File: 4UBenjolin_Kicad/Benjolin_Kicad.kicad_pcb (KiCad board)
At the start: 2 copper layers, 177.8 x 59.9 mm, 106 parts, among them J1 Conn_01x03_Female, J10 MAINOUT, J11 PWM, J12 RUN, J13 XOR, J14 CV_1, J15 CV_2, J4 EXT.INPUT, J5 CV_F, J6 PUL2, J7 TRI1, J8 TRI2, J9 PUL1, P10R1 10k, P11R1 10k, P1R1 10k, P2R1 10k, P3R1 10k, P4R1 10k, P5R1 10k, P6R1 10k, P8R1 10k, P9R1 10k, Q1 BC547, SW1 SW_SPDT, U1 TL074, U2 TL072, U3 TL074, U4 TL074, U5 SSI2164, U6 4021, U7 L78L09_SOT89

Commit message: Added footprint for Banana Panel Cutout and built up a generic 4u Front Panel
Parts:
- removed C1, C11, C14, C16, C17: 100n, Capacitor_SMD:C_1206_3216Metric_Pad1.42x1.75mm_HandSolder
- removed C10, C5, C8: 220p, Capacitor_SMD:C_1206_3216Metric_Pad1.42x1.75mm_HandSolder
- removed C12, C13, C15, C18: 10uf, Capacitor_THT:CP_Radial_D5.0mm_P2.50mm
- removed C2, C3, C4, C9: 560p, Capacitor_SMD:C_1206_3216Metric_Pad1.42x1.75mm_HandSolder
- removed C6, C7: 1n, Capacitor_SMD:C_1206_3216Metric_Pad1.42x1.75mm_HandSolder
- removed D1, D2, D3, D4, D5, D6: 1N914, Diode_THT:D_DO-35_SOD27_P2.54mm_Vertical_AnodeUp
- removed J1: Conn_01x03_Female, Connector_PinSocket_2.54mm:PinSocket_1x03_P2.54mm_Vertical
- removed J10: MAINOUT, Connector_Audio:Jack_3.5mm_QingPu_WQP-PJ398SM_Vertical_CircularHoles
- removed J11: PWM, Connector_Audio:Jack_3.5mm_QingPu_WQP-PJ398SM_Vertical_CircularHoles
- removed J12: RUN, Connector_Audio:Jack_3.5mm_QingPu_WQP-PJ398SM_Vertical_CircularHoles
- removed J13: XOR, Connector_Audio:Jack_3.5mm_QingPu_WQP-PJ398SM_Vertical_CircularHoles
- removed J14: CV_1, Connector_Audio:Jack_3.5mm_QingPu_WQP-PJ398SM_Vertical_CircularHoles
- removed J15: CV_2, Connector_Audio:Jack_3.5mm_QingPu_WQP-PJ398SM_Vertical_CircularHoles
- removed J4: EXT.INPUT, Connector_Audio:Jack_3.5mm_QingPu_WQP-PJ398SM_Vertical_CircularHoles
- removed J5: CV_F, Connector_Audio:Jack_3.5mm_QingPu_WQP-PJ398SM_Vertical_CircularHoles
- removed J6: PUL2, Connector_Audio:Jack_3.5mm_QingPu_WQP-PJ398SM_Vertical_CircularHoles
- removed J7: TRI1, Connector_Audio:Jack_3.5mm_QingPu_WQP-PJ398SM_Vertical_CircularHoles
- removed J8: TRI2, Connector_Audio:Jack_3.5mm_QingPu_WQP-PJ398SM_Vertical_CircularHoles
- removed J9: PUL1, Connector_Audio:Jack_3.5mm_QingPu_WQP-PJ398SM_Vertical_CircularHoles
- removed P10R1, P11R1, P1R1, P2R1, P3R1, P4R1, P5R1, P6R1, P8R1, P9R1: 10k, Potentiometer_THT:Potentiometer_Alps_RK09K_Single_Vertical
- removed Q1: BC547, Package_TO_SOT_THT:TO-92_Inline
- removed R1, R16: 62k, Resistor_SMD:R_0603_1608Metric_Pad1.05x0.95mm_HandSolder
- removed R10, R17, R28, R29, R3, R30, R4, R6, R7: 51k, Resistor_SMD:R_0603_1608Metric_Pad1.05x0.95mm_HandSolder
- removed R11: 150k, Resistor_SMD:R_0603_1608Metric_Pad1.05x0.95mm_HandSolder
- removed R12, R13, R14, R33, R49: 10k, Resistor_SMD:R_0603_1608Metric_Pad1.05x0.95mm_HandSolder
- removed R15, R2, R20, R21, R22, R34, R37, R38, R39, R42, R45, R47, R48, R5, R8: 30k, Resistor_SMD:R_0603_1608Metric_Pad1.05x0.95mm_HandSolder
- removed R18, R31, R32, R35, R36, R9: 100k, Resistor_SMD:R_0603_1608Metric_Pad1.05x0.95mm_HandSolder
- removed R19, R26, R40, R41, R43, R44: 15k, Resistor_SMD:R_0603_1608Metric_Pad1.05x0.95mm_HandSolder
- removed R23, R24, R25, R46: 510r, Resistor_SMD:R_0603_1608Metric_Pad1.05x0.95mm_HandSolder
- removed R27: 1.5k, Resistor_SMD:R_0603_1608Metric_Pad1.05x0.95mm_HandSolder
- removed R50: 470k, Resistor_SMD:R_0603_1608Metric_Pad1.05x0.95mm_HandSolder
- removed SW1: SW_SPDT, Connector_PinSocket_2.54mm:PinSocket_1x03_P2.54mm_Vertical
- removed U1, U3, U4: TL074, Package_SO:SOIC-14_3.9x8.7mm_P1.27mm
- removed U2: TL072, Package_SO:SOIC-8_3.9x4.9mm_P1.27mm
- removed U5: SSI2164, Package_SO:SOIC-16_3.9x9.9mm_P1.27mm
- removed U6: 4021, Package_SO:SOIC-16_3.9x9.9mm_P1.27mm
- removed U7: L78L09_SOT89, Package_TO_SOT_THT:TO-92L_Inline
- added REF**: Banana Jack, SynthComponents:Cinch Banana Jack (Panel), F.Cu at (92.1, 128.6)
- added REF**: Banana Jack, SynthComponents:Cinch Banana Jack (Panel), F.Cu at (117.5, 109.5)
- added REF**: Banana Jack, SynthComponents:Cinch Banana Jack (Panel), F.Cu at (92.1, 109.5)
- added REF**: Banana Jack, SynthComponents:Cinch Banana Jack (Panel), F.Cu at (41.3, 128.6)
- added REF**: Banana Jack, SynthComponents:Cinch Banana Jack (Panel), F.Cu at (117.5, 147.6)
- added REF**: Banana Jack, SynthComponents:Cinch Banana Jack (Panel), F.Cu at (66.7, 128.6)
- added REF**: Banana Jack, SynthComponents:Cinch Banana Jack (Panel), F.Cu at (92.1, 166.7)
- added REF**: Banana Jack, SynthComponents:Cinch Banana Jack (Panel), F.Cu at (117.5, 128.6)
- added REF**: Banana Jack, SynthComponents:Cinch Banana Jack (Panel), F.Cu at (41.3, 52.4)
- added REF**: Banana Jack, SynthComponents:Cinch Banana Jack (Panel), F.Cu at (66.7, 52.4)
- added REF**: Banana Jack, SynthComponents:Cinch Banana Jack (Panel), F.Cu at (92.1, 52.4)
- added REF**: Banana Jack, SynthComponents:Cinch Banana Jack (Panel), F.Cu at (66.7, 166.7)
- added REF**: Banana Jack, SynthComponents:Cinch Banana Jack (Panel), F.Cu at (117.5, 71.4)
- added REF**: Banana Jack, SynthComponents:Cinch Banana Jack (Panel), F.Cu at (117.5, 90.5)
- added REF**: Banana Jack, SynthComponents:Cinch Banana Jack (Panel), F.Cu at (92.1, 90.5)
- added REF**: Banana Jack, SynthComponents:Cinch Banana Jack (Panel), F.Cu at (66.7, 90.5)
- added REF**: Banana Jack, SynthComponents:Cinch Banana Jack (Panel), F.Cu at (41.3, 90.5)
- added REF**: Banana Jack, SynthComponents:Cinch Banana Jack (Panel), F.Cu at (41.3, 71.4)
- added REF**: Banana Jack, SynthComponents:Cinch Banana Jack (Panel), F.Cu at (66.7, 71.4)
- added REF**: Banana Jack, SynthComponents:Cinch Banana Jack (Panel), F.Cu at (92.1, 71.4)
- added REF**: Banana Jack, SynthComponents:Cinch Banana Jack (Panel), F.Cu at (117.5, 52.4)
- added REF**: Banana Jack, SynthComponents:Cinch Banana Jack (Panel), F.Cu at (117.5, 33.3)
- added REF**: Banana Jack, SynthComponents:Cinch Banana Jack (Panel), F.Cu at (41.3, 166.7)
- added REF**: Banana Jack, SynthComponents:Cinch Banana Jack (Panel), F.Cu at (41.3, 33.3)
- added REF**: Banana Jack, SynthComponents:Cinch Banana Jack (Panel), F.Cu at (66.7, 33.3)
- added REF**: Banana Jack, SynthComponents:Cinch Banana Jack (Panel), F.Cu at (92.1, 33.3)
- added REF**: Banana Jack, SynthComponents:Cinch Banana Jack (Panel), F.Cu at (41.3, 147.6)
- added REF**: Banana Jack, SynthComponents:Cinch Banana Jack (Panel), F.Cu at (66.7, 147.6)
- added REF**: Banana Jack, SynthComponents:Cinch Banana Jack (Panel), F.Cu at (92.1, 147.6)
- added REF**: Banana Jack, SynthComponents:Cinch Banana Jack (Panel), F.Cu at (66.7, 109.5)
- added REF**: Banana Jack, SynthComponents:Cinch Banana Jack (Panel), F.Cu at (41.3, 109.5)
- added REF**: Banana Jack, SynthComponents:Cinch Banana Jack (Panel), F.Cu at (117.5, 166.7)
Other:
- board size 177.8 x 59.9 mm -> 107.9 x 177.5 mm
- board text added: "4mm hole"

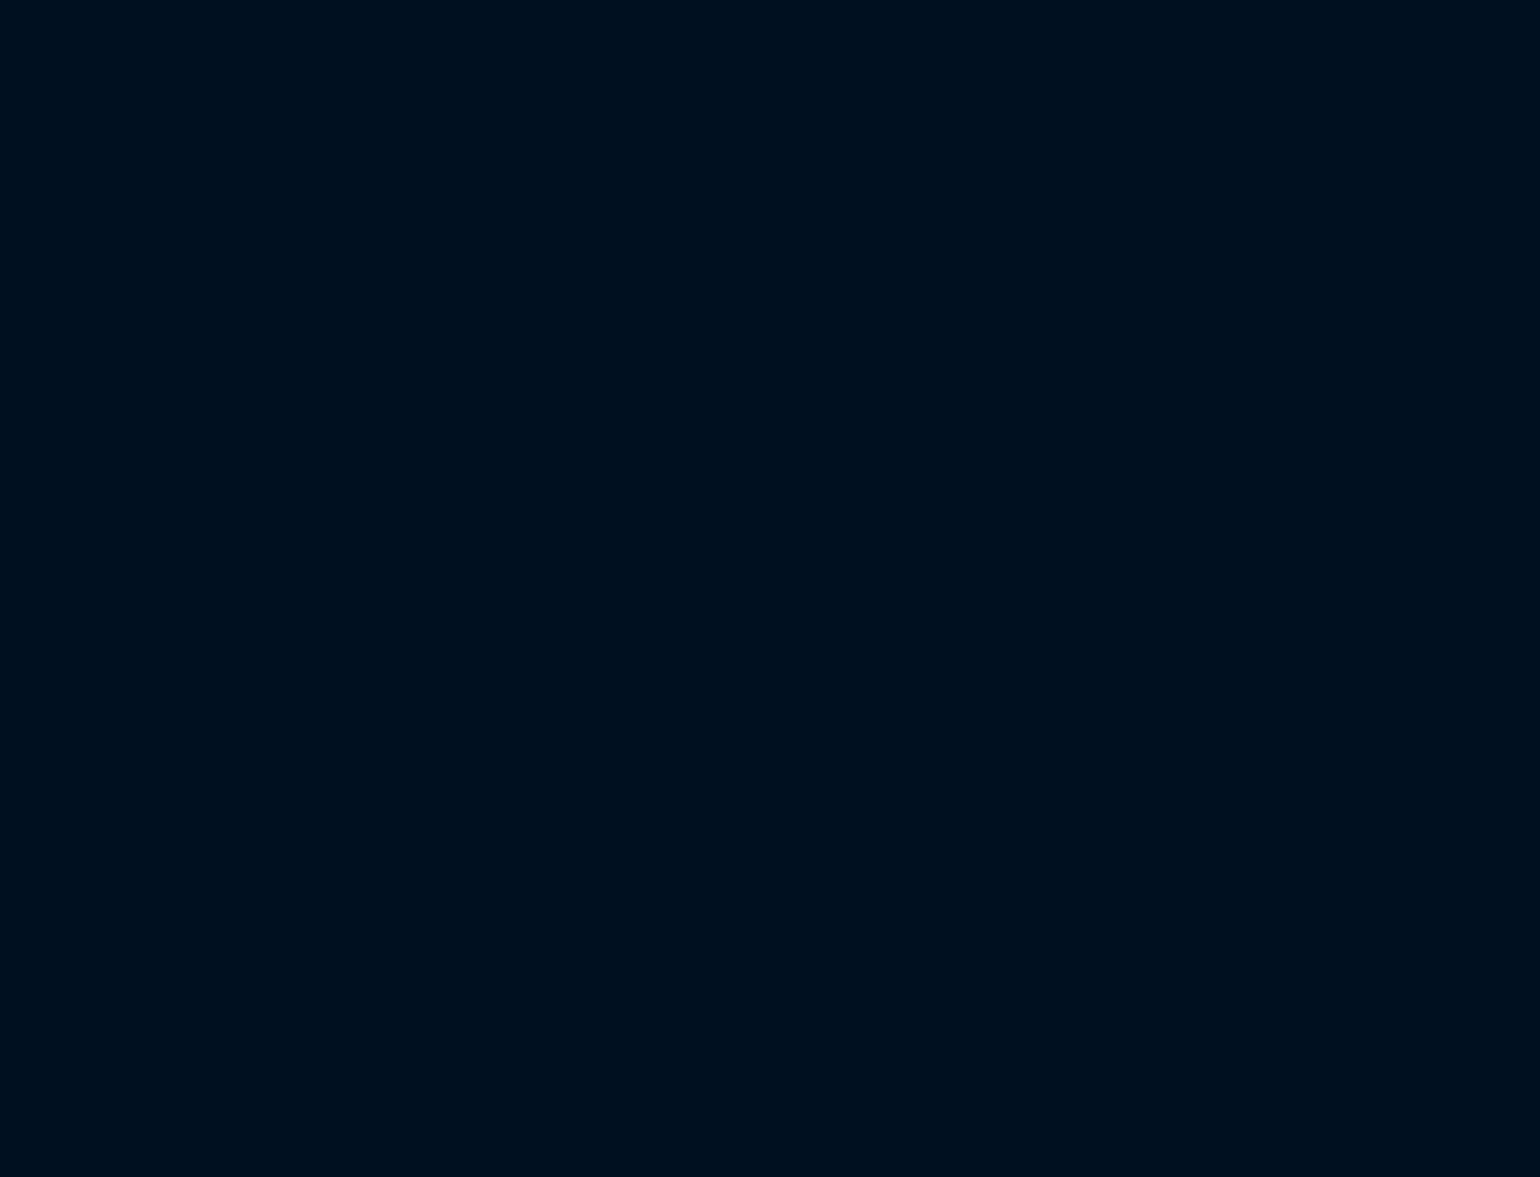
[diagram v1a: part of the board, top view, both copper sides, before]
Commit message: Added footprints for banana PCB and made pcb size
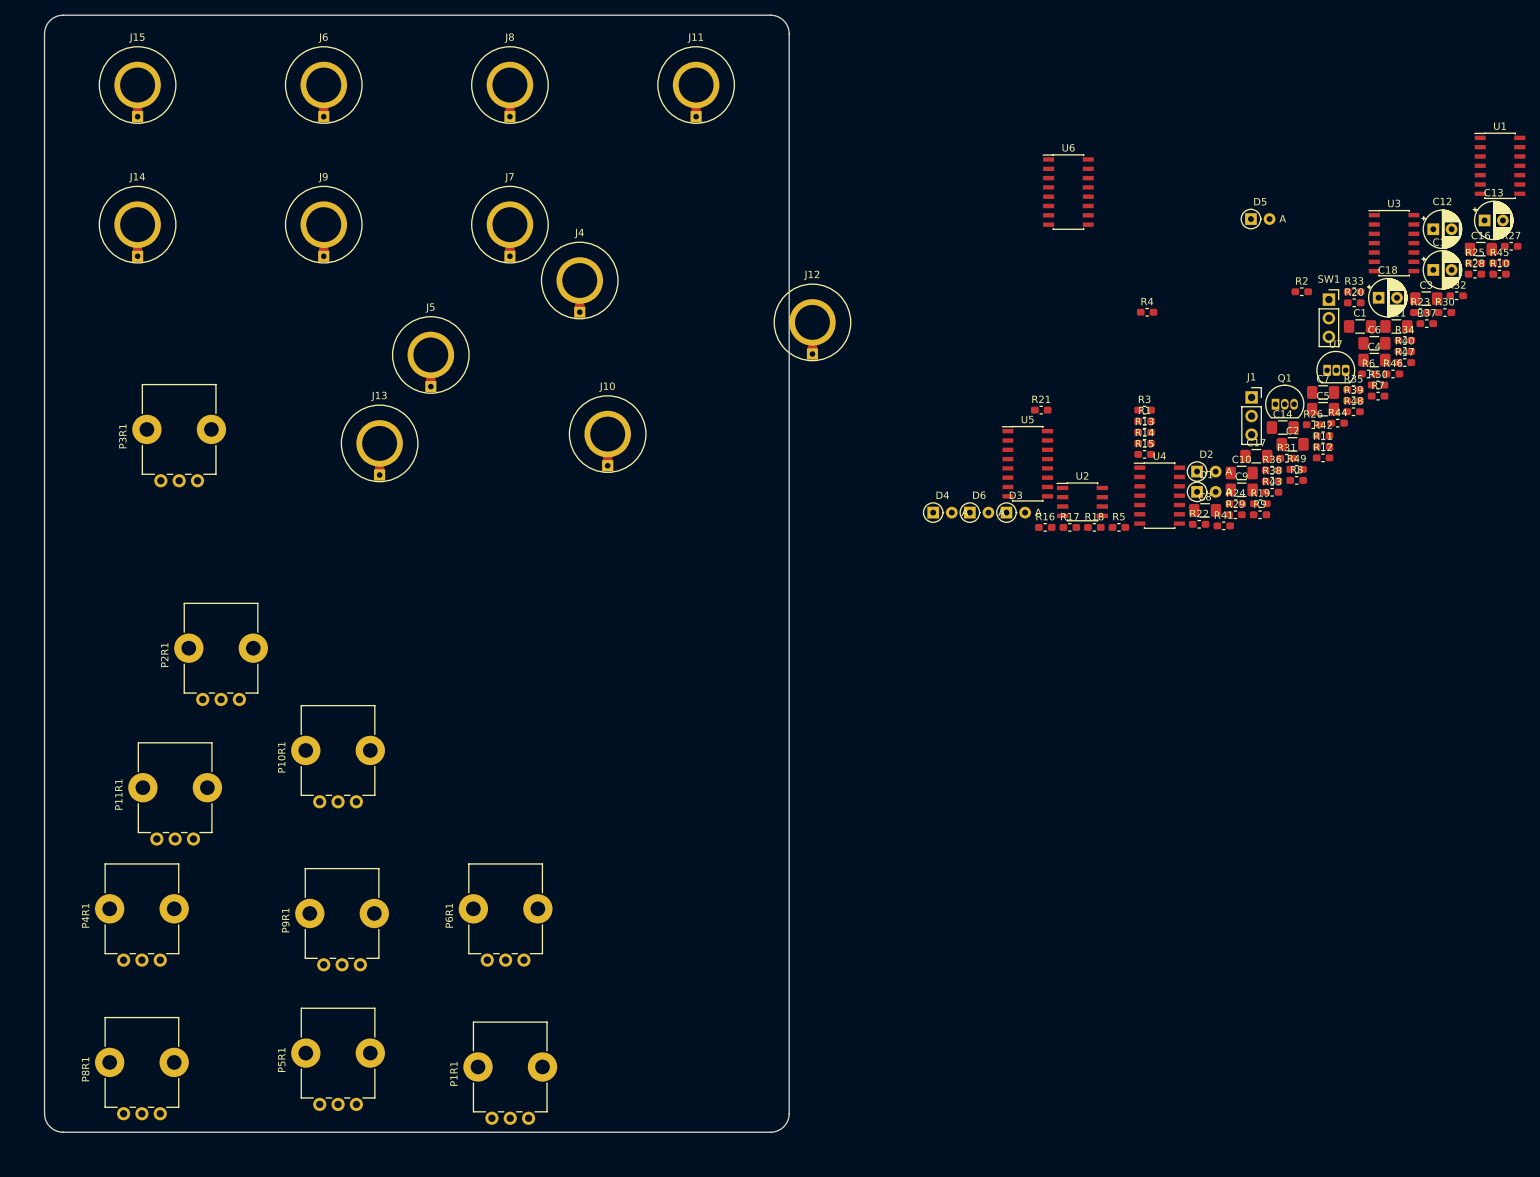
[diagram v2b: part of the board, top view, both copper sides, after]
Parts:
- added C1: 100n, Capacitor_SMD:C_1206_3216Metric_Pad1.42x1.75mm_HandSolder, F.Cu at (357.3, 55.2)
- added C10: 220p, Capacitor_SMD:C_1206_3216Metric_Pad1.42x1.75mm_HandSolder, F.Cu at (341.1, 75.2)
- added C11: 100n, Capacitor_SMD:C_1206_3216Metric_Pad1.42x1.75mm_HandSolder, F.Cu at (362.2, 55.2)
- added C12: 10uf, Capacitor_THT:CP_Radial_D5.0mm_P2.50mm, F.Cu at (367.3, 41.9)
- added C13: 10uf, Capacitor_THT:CP_Radial_D5.0mm_P2.50mm, F.Cu at (374.3, 40.7)
- added C14: 100n, Capacitor_SMD:C_1206_3216Metric_Pad1.42x1.75mm_HandSolder, F.Cu at (346.7, 69.0)
- added C15: 10uf, Capacitor_THT:CP_Radial_D5.0mm_P2.50mm, F.Cu at (367.3, 47.5)
- added C16: 100n, Capacitor_SMD:C_1206_3216Metric_Pad1.42x1.75mm_HandSolder, F.Cu at (373.8, 44.6)
- added C17: 100n, Capacitor_SMD:C_1206_3216Metric_Pad1.42x1.75mm_HandSolder, F.Cu at (343.1, 72.9)
- added C18: 10uf, Capacitor_THT:CP_Radial_D5.0mm_P2.50mm, F.Cu at (359.8, 51.3)
- added C2: 560p, Capacitor_SMD:C_1206_3216Metric_Pad1.42x1.75mm_HandSolder, F.Cu at (348.1, 71.3)
- added C3: 560p, Capacitor_SMD:C_1206_3216Metric_Pad1.42x1.75mm_HandSolder, F.Cu at (366.3, 51.4)
- added C4: 560p, Capacitor_SMD:C_1206_3216Metric_Pad1.42x1.75mm_HandSolder, F.Cu at (359.2, 59.8)
- added C5: 220p, Capacitor_SMD:C_1206_3216Metric_Pad1.42x1.75mm_HandSolder, F.Cu at (352.2, 66.5)
- added C6: 1n, Capacitor_SMD:C_1206_3216Metric_Pad1.42x1.75mm_HandSolder, F.Cu at (359.2, 57.5)
- added C7: 1n, Capacitor_SMD:C_1206_3216Metric_Pad1.42x1.75mm_HandSolder, F.Cu at (352.2, 64.2)
- added C8: 220p, Capacitor_SMD:C_1206_3216Metric_Pad1.42x1.75mm_HandSolder, F.Cu at (336.1, 80.3)
- added C9: 560p, Capacitor_SMD:C_1206_3216Metric_Pad1.42x1.75mm_HandSolder, F.Cu at (341.1, 77.5)
- added D1: 1N914, Diode_THT:D_DO-35_SOD27_P2.54mm_Vertical_AnodeUp, F.Cu at (335.0, 77.7)
- added D2: 1N914, Diode_THT:D_DO-35_SOD27_P2.54mm_Vertical_AnodeUp, F.Cu at (335.0, 75.0)
- added D3: 1N914, Diode_THT:D_DO-35_SOD27_P2.54mm_Vertical_AnodeUp, F.Cu at (309.0, 80.6)
- added D4: 1N914, Diode_THT:D_DO-35_SOD27_P2.54mm_Vertical_AnodeUp, F.Cu at (299.0, 80.6)
- added D5: 1N914, Diode_THT:D_DO-35_SOD27_P2.54mm_Vertical_AnodeUp, F.Cu at (342.4, 40.5)
- added D6: 1N914, Diode_THT:D_DO-35_SOD27_P2.54mm_Vertical_AnodeUp, F.Cu at (304.0, 80.6)
- added J1: Conn_01x03_Female, Connector_PinSocket_2.54mm:PinSocket_1x03_P2.54mm_Vertical, F.Cu at (342.5, 64.9)
- added J10: MAINOUT, SynthComponents:Banana_Jack_PCB, F.Cu at (254.6, 69.8)
- added J11: PWM, SynthComponents:Banana_Jack_PCB, F.Cu at (266.7, 22.2)
- added J12: RUN, SynthComponents:Banana_Jack_PCB, F.Cu at (282.6, 54.6)
- added J13: XOR, SynthComponents:Banana_Jack_PCB, F.Cu at (223.5, 71.1)
- added J14: CV_1, SynthComponents:Banana_Jack_PCB, F.Cu at (190.5, 41.3)
- added J15: CV_2, SynthComponents:Banana_Jack_PCB, F.Cu at (190.5, 22.2)
- added J4: EXT.INPUT, SynthComponents:Banana_Jack_PCB, F.Cu at (250.8, 48.9)
- added J5: CV_F, SynthComponents:Banana_Jack_PCB, F.Cu at (230.5, 59.1)
- added J6: PUL2, SynthComponents:Banana_Jack_PCB, F.Cu at (215.9, 22.2)
- added J7: TRI1, SynthComponents:Banana_Jack_PCB, F.Cu at (241.3, 41.3)
- added J8: TRI2, SynthComponents:Banana_Jack_PCB, F.Cu at (241.3, 22.2)
- added J9: PUL1, SynthComponents:Banana_Jack_PCB, F.Cu at (215.9, 41.3)
- added P10R1: 10k, Potentiometer_THT:Potentiometer_Alps_RK09K_Single_Vertical, F.Cu at (220.3, 120.0)
- added P11R1: 10k, Potentiometer_THT:Potentiometer_Alps_RK09K_Single_Vertical, F.Cu at (198.1, 125.1)
- added P1R1: 10k, Potentiometer_THT:Potentiometer_Alps_RK09K_Single_Vertical, F.Cu at (243.8, 163.2)
- added P2R1: 10k, Potentiometer_THT:Potentiometer_Alps_RK09K_Single_Vertical, F.Cu at (204.4, 106.1)
- added P3R1: 10k, Potentiometer_THT:Potentiometer_Alps_RK09K_Single_Vertical, F.Cu at (198.7, 76.2)
- added P4R1: 10k, Potentiometer_THT:Potentiometer_Alps_RK09K_Single_Vertical, F.Cu at (193.6, 141.6)
- added P5R1: 10k, Potentiometer_THT:Potentiometer_Alps_RK09K_Single_Vertical, F.Cu at (220.3, 161.3)
- added P6R1: 10k, Potentiometer_THT:Potentiometer_Alps_RK09K_Single_Vertical, F.Cu at (243.2, 141.6)
- added P8R1: 10k, Potentiometer_THT:Potentiometer_Alps_RK09K_Single_Vertical, F.Cu at (193.6, 162.6)
- added P9R1: 10k, Potentiometer_THT:Potentiometer_Alps_RK09K_Single_Vertical, F.Cu at (220.9, 142.3)
- added Q1: BC547, Package_TO_SOT_THT:TO-92_Inline, F.Cu at (345.7, 65.8)
- added R1: 62k, Resistor_SMD:R_0603_1608Metric_Pad1.05x0.95mm_HandSolder, F.Cu at (327.9, 68.1)
- added R10: 51k, Resistor_SMD:R_0603_1608Metric_Pad1.05x0.95mm_HandSolder, F.Cu at (376.3, 48.0)
- added R11: 150k, Resistor_SMD:R_0603_1608Metric_Pad1.05x0.95mm_HandSolder, F.Cu at (352.2, 71.6)
- added R12: 10k, Resistor_SMD:R_0603_1608Metric_Pad1.05x0.95mm_HandSolder, F.Cu at (352.2, 73.1)
- added R13: 10k, Resistor_SMD:R_0603_1608Metric_Pad1.05x0.95mm_HandSolder, F.Cu at (327.9, 69.6)
- added R14: 10k, Resistor_SMD:R_0603_1608Metric_Pad1.05x0.95mm_HandSolder, F.Cu at (327.9, 71.1)
- added R15: 30k, Resistor_SMD:R_0603_1608Metric_Pad1.05x0.95mm_HandSolder, F.Cu at (327.9, 72.6)
- added R16: 62k, Resistor_SMD:R_0603_1608Metric_Pad1.05x0.95mm_HandSolder, F.Cu at (314.3, 82.6)
- added R17: 51k, Resistor_SMD:R_0603_1608Metric_Pad1.05x0.95mm_HandSolder, F.Cu at (317.7, 82.6)
- added R18: 100k, Resistor_SMD:R_0603_1608Metric_Pad1.05x0.95mm_HandSolder, F.Cu at (321.0, 82.6)
- added R19: 15k, Resistor_SMD:R_0603_1608Metric_Pad1.05x0.95mm_HandSolder, F.Cu at (343.7, 79.4)
- added R2: 30k, Resistor_SMD:R_0603_1608Metric_Pad1.05x0.95mm_HandSolder, F.Cu at (349.3, 50.4)
- added R20: 30k, Resistor_SMD:R_0603_1608Metric_Pad1.05x0.95mm_HandSolder, F.Cu at (356.5, 51.9)
- added R21: 30k, Resistor_SMD:R_0603_1608Metric_Pad1.05x0.95mm_HandSolder, F.Cu at (313.8, 66.6)
- added R22: 30k, Resistor_SMD:R_0603_1608Metric_Pad1.05x0.95mm_HandSolder, F.Cu at (335.3, 82.2)
- added R23: 510r, Resistor_SMD:R_0603_1608Metric_Pad1.05x0.95mm_HandSolder, F.Cu at (365.5, 53.3)
- added R24: 510r, Resistor_SMD:R_0603_1608Metric_Pad1.05x0.95mm_HandSolder, F.Cu at (340.3, 79.4)
- added R25: 510r, Resistor_SMD:R_0603_1608Metric_Pad1.05x0.95mm_HandSolder, F.Cu at (373.0, 46.5)
- added R26: 15k, Resistor_SMD:R_0603_1608Metric_Pad1.05x0.95mm_HandSolder, F.Cu at (350.9, 68.6)
- added R27: 1.5k, Resistor_SMD:R_0603_1608Metric_Pad1.05x0.95mm_HandSolder, F.Cu at (377.9, 44.2)
- added R28: 51k, Resistor_SMD:R_0603_1608Metric_Pad1.05x0.95mm_HandSolder, F.Cu at (373.0, 48.0)
- added R29: 51k, Resistor_SMD:R_0603_1608Metric_Pad1.05x0.95mm_HandSolder, F.Cu at (340.3, 80.9)
- added R3: 51k, Resistor_SMD:R_0603_1608Metric_Pad1.05x0.95mm_HandSolder, F.Cu at (327.9, 66.6)
- added R30: 51k, Resistor_SMD:R_0603_1608Metric_Pad1.05x0.95mm_HandSolder, F.Cu at (368.9, 53.3)
- added R31: 100k, Resistor_SMD:R_0603_1608Metric_Pad1.05x0.95mm_HandSolder, F.Cu at (347.3, 73.2)
- added R32: 100k, Resistor_SMD:R_0603_1608Metric_Pad1.05x0.95mm_HandSolder, F.Cu at (370.5, 51.0)
- added R33: 10k, Resistor_SMD:R_0603_1608Metric_Pad1.05x0.95mm_HandSolder, F.Cu at (356.5, 50.4)
- added R34: 30k, Resistor_SMD:R_0603_1608Metric_Pad1.05x0.95mm_HandSolder, F.Cu at (363.4, 57.1)
- added R35: 100k, Resistor_SMD:R_0603_1608Metric_Pad1.05x0.95mm_HandSolder, F.Cu at (356.4, 63.8)
- added R36: 100k, Resistor_SMD:R_0603_1608Metric_Pad1.05x0.95mm_HandSolder, F.Cu at (345.3, 74.8)
- added R37: 30k, Resistor_SMD:R_0603_1608Metric_Pad1.05x0.95mm_HandSolder, F.Cu at (366.4, 54.8)
- added R38: 30k, Resistor_SMD:R_0603_1608Metric_Pad1.05x0.95mm_HandSolder, F.Cu at (345.3, 76.3)
- added R39: 30k, Resistor_SMD:R_0603_1608Metric_Pad1.05x0.95mm_HandSolder, F.Cu at (356.4, 65.3)
- added R4: 51k, Resistor_SMD:R_0603_1608Metric_Pad1.05x0.95mm_HandSolder, F.Cu at (328.2, 53.2)
- added R40: 15k, Resistor_SMD:R_0603_1608Metric_Pad1.05x0.95mm_HandSolder, F.Cu at (363.4, 58.6)
- added R41: 15k, Resistor_SMD:R_0603_1608Metric_Pad1.05x0.95mm_HandSolder, F.Cu at (338.7, 82.4)
- added R42: 30k, Resistor_SMD:R_0603_1608Metric_Pad1.05x0.95mm_HandSolder, F.Cu at (352.2, 70.1)
- added R43: 15k, Resistor_SMD:R_0603_1608Metric_Pad1.05x0.95mm_HandSolder, F.Cu at (345.3, 77.8)
- added R44: 15k, Resistor_SMD:R_0603_1608Metric_Pad1.05x0.95mm_HandSolder, F.Cu at (354.2, 68.4)
- added R45: 30k, Resistor_SMD:R_0603_1608Metric_Pad1.05x0.95mm_HandSolder, F.Cu at (376.3, 46.5)
- added R46: 510r, Resistor_SMD:R_0603_1608Metric_Pad1.05x0.95mm_HandSolder, F.Cu at (361.8, 61.7)
- added R47: 30k, Resistor_SMD:R_0603_1608Metric_Pad1.05x0.95mm_HandSolder, F.Cu at (363.4, 60.1)
- added R48: 30k, Resistor_SMD:R_0603_1608Metric_Pad1.05x0.95mm_HandSolder, F.Cu at (356.4, 66.8)
- added R49: 10k, Resistor_SMD:R_0603_1608Metric_Pad1.05x0.95mm_HandSolder, F.Cu at (348.6, 74.7)
- added R5: 30k, Resistor_SMD:R_0603_1608Metric_Pad1.05x0.95mm_HandSolder, F.Cu at (324.4, 82.6)
- added R50: 470k, Resistor_SMD:R_0603_1608Metric_Pad1.05x0.95mm_HandSolder, F.Cu at (359.7, 63.2)
- added R6: 51k, Resistor_SMD:R_0603_1608Metric_Pad1.05x0.95mm_HandSolder, F.Cu at (358.4, 61.7)
- added R7: 51k, Resistor_SMD:R_0603_1608Metric_Pad1.05x0.95mm_HandSolder, F.Cu at (359.7, 64.7)
- added R8: 30k, Resistor_SMD:R_0603_1608Metric_Pad1.05x0.95mm_HandSolder, F.Cu at (348.6, 76.2)
- added R9: 100k, Resistor_SMD:R_0603_1608Metric_Pad1.05x0.95mm_HandSolder, F.Cu at (343.6, 80.9)
- added SW1: SW_SPDT, Connector_PinSocket_2.54mm:PinSocket_1x03_P2.54mm_Vertical, F.Cu at (353.0, 51.5)
- added U1: TL074, Package_SO:SOIC-14_3.9x8.7mm_P1.27mm, F.Cu at (376.4, 33.3)
- added U2: TL072, Package_SO:SOIC-8_3.9x4.9mm_P1.27mm, F.Cu at (319.4, 79.1)
- added U3: TL074, Package_SO:SOIC-14_3.9x8.7mm_P1.27mm, F.Cu at (361.9, 43.8)
- added U4: TL074, Package_SO:SOIC-14_3.9x8.7mm_P1.27mm, F.Cu at (329.9, 78.3)
- added U5: SSI2164, Package_SO:SOIC-16_3.9x9.9mm_P1.27mm, F.Cu at (311.9, 73.9)
- added U6: 4021, Package_SO:SOIC-16_3.9x9.9mm_P1.27mm, F.Cu at (317.5, 36.8)
- added U7: L78L09_SOT89, Package_TO_SOT_THT:TO-92L_Inline, F.Cu at (352.8, 61.2)
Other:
- board size 107.9 x 177.5 mm -> 254 x 177.5 mm
